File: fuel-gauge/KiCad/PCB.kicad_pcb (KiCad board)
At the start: 2 copper layers, 100.1 x 70 mm, 39 parts, among them P1 CONN_01X04, P2 CONN_01X04, P3 CONN_01X04, Q1 BSS84, Q2 BSS138, Q3 2N7002, SW1 Switch_SPDT_x2, U1 AQV252G, U2 SN74LVC1G08DBVR, U3 TLV3691IDCKR, U4 bq34z100pw

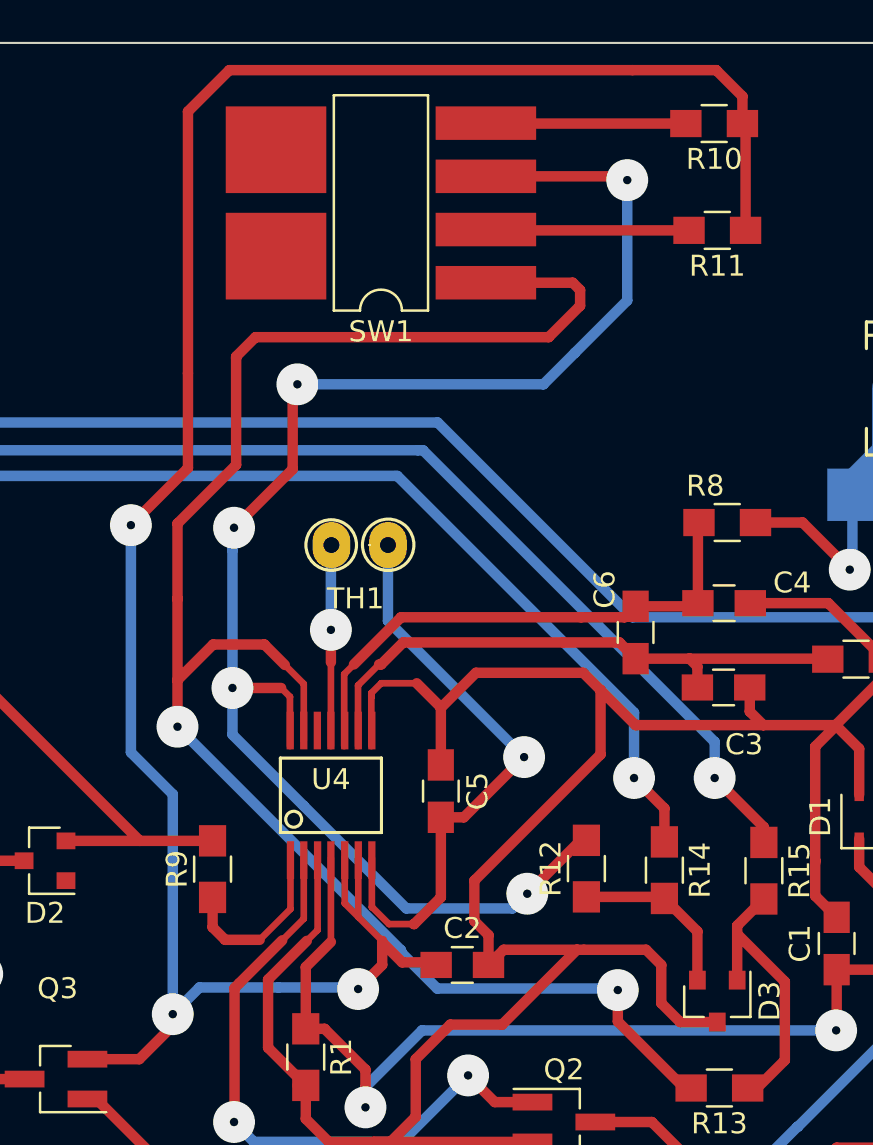
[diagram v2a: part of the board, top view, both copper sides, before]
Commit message: Correct the footprint of the switch 1
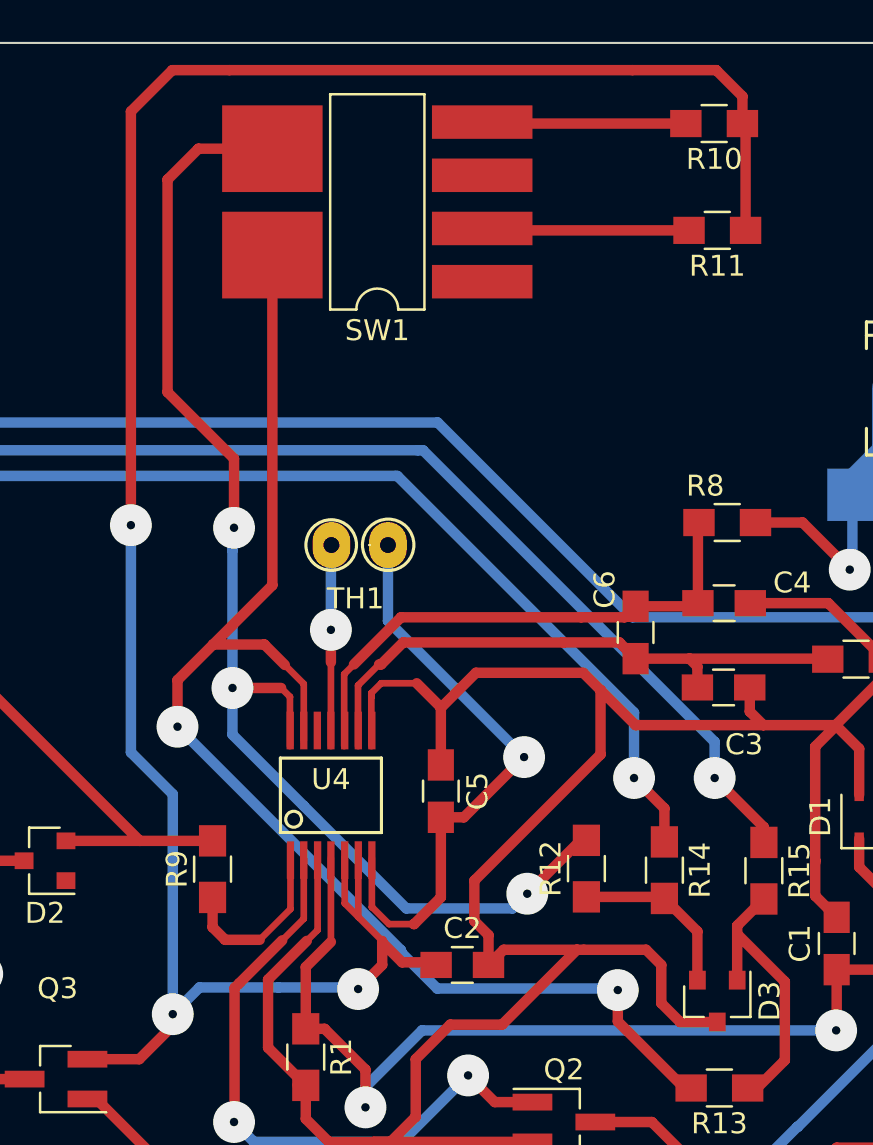
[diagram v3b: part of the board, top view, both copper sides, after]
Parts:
- moved SW1 0.18 mm to (157.6, 71.3)
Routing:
- net Net-(R13-Pad2): track 84.6 -> 64.9 mm
- net Net-(R12-Pad2): track 75.0 -> 60.5 mm, vias 5 -> 3
- net REG_IN: track 107.8 -> 109.4 mm

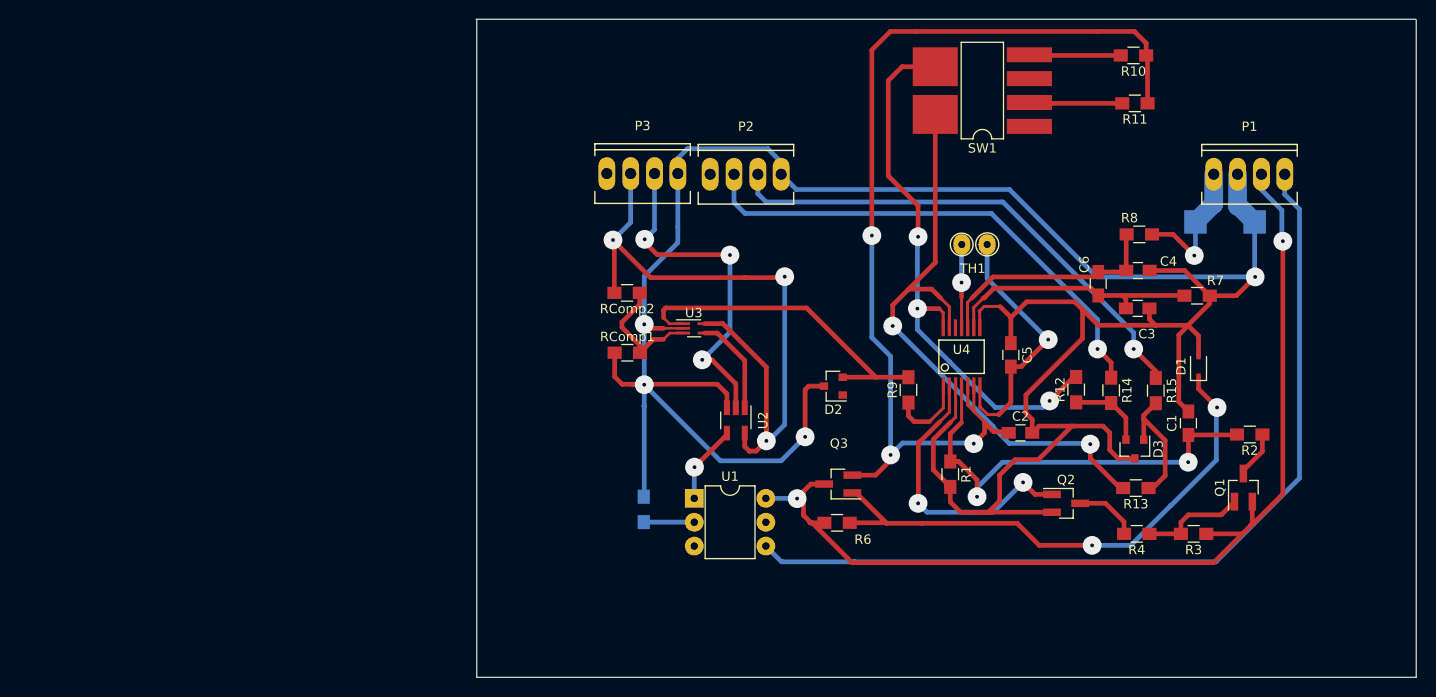
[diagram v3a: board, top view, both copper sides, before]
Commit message: Update the design to the v2
Include new routing to minimize the number of vias used and some
electrical considerations. Also the names of the connectors and the
positions of the switch.
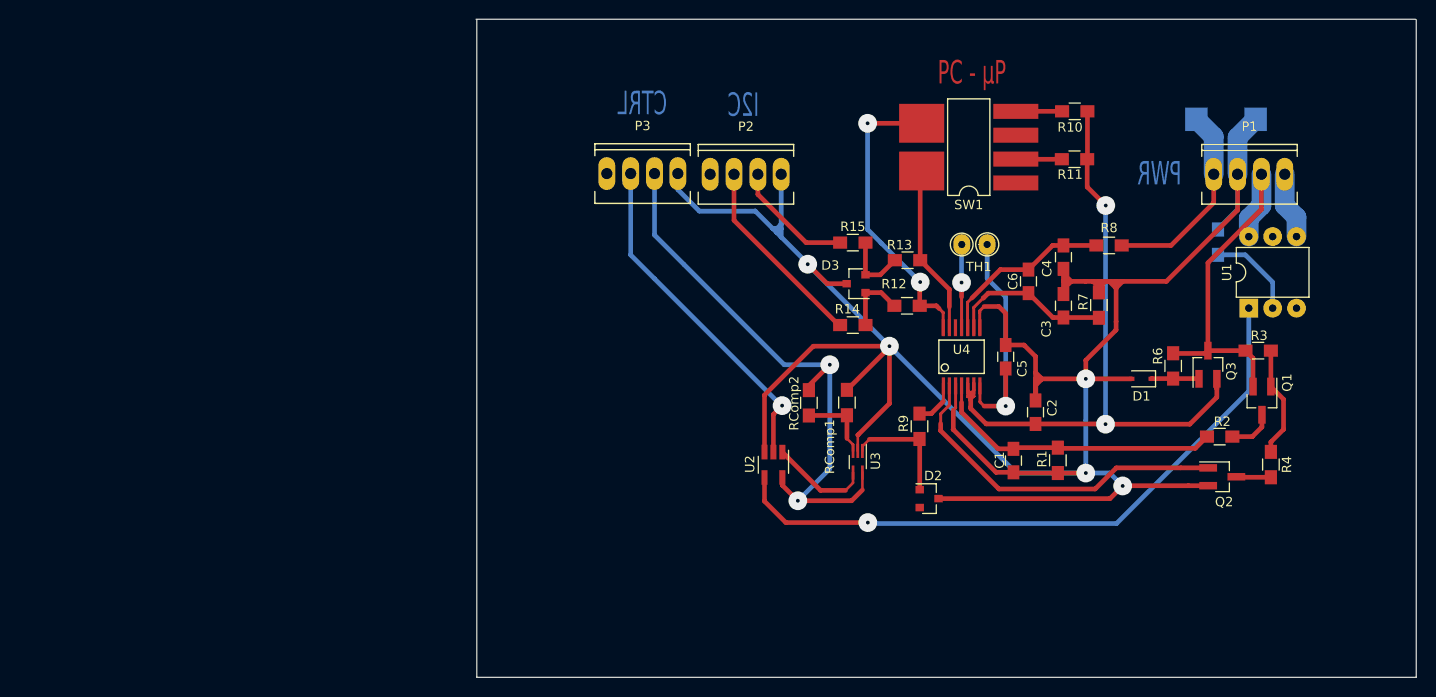
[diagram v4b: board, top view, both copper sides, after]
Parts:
- moved RRy1 67.4 mm to (178.9, 83.7)
- moved U1 62.4 mm to (182.2, 90.7), turned to 90 degrees
- moved Q3 41.3 mm to (177.8, 96.7), turned to 90 degrees
- moved R6 39.5 mm to (174.1, 96.8), turned to 270 degrees
- moved R15 35.9 mm to (140.0, 83.7), turned to 0 degrees
- moved D3 34.5 mm to (140.4, 88.1), turned to 180 degrees
- moved R13 34.3 mm to (145.8, 85.6), turned to 0 degrees
- moved R14 28.4 mm to (140.0, 92.5), turned to 0 degrees
- moved RComp1 24.0 mm to (139.4, 100.8), turned to 270 degrees
- moved RComp2 22.6 mm to (135.3, 100.8), turned to 90 degrees
- moved U3 22.1 mm to (140.3, 107.0), turned to 270 degrees
- moved R3 20.7 mm to (183.2, 95.2), turned to 0 degrees
- moved R12 20.1 mm to (145.8, 90.5), turned to 0 degrees
- moved C1 19.0 mm to (157.1, 106.9), turned to 270 degrees
- moved Q2 16.9 mm to (179.3, 108.7)
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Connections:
- D2 pad 1: Net-(D2-Pad1) -> (no net)
- D2 pad 2: (no net) -> Net-(D2-Pad2)
- P3 pad 2: +5V -> Net-(P3-Pad2)
- P3 pad 3: Net-(P3-Pad3) -> +5V
- R12 pad 1: Net-(D3-Pad1) -> Net-(D3-Pad2)
- R13 pad 1: Net-(D3-Pad2) -> Net-(D3-Pad1)
- R14 pad 2: Net-(D3-Pad1) -> Net-(D3-Pad2)
- R15 pad 2: Net-(D3-Pad2) -> Net-(D3-Pad1)
- R9 pad 2: Net-(D2-Pad1) -> Net-(D2-Pad2)
- U2 pad 2: Net-(P3-Pad3) -> Net-(P3-Pad2)
- U3 pad 1: Net-(D2-Pad1) -> Net-(D2-Pad2)
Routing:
- net /PUSHBUTTON: track 94.3 -> 8.14 mm
- net /BATT+: track 110.2 -> 40.3 mm, vias 2 -> 0
- net Net-(U1-Pad1): track 8.39 -> 69.7 mm
- net Net-(D1-Pad1): track 58.6 -> 5.10 mm, vias 2 -> 0
- net Net-(R13-Pad2): track 64.9 -> 18.5 mm, vias 2 -> 0
- net /SCL: track 54.0 -> 13.0 mm, vias 1 -> 0
- net Net-(P3-Pad3): track 36.9 -> 0.00 mm, vias 3 -> 0
- net Net-(P3-Pad2): track 0.00 -> 36.8 mm, vias 0 -> 1
- net Net-(D2-Pad1): track 35.9 -> 0.00 mm
- net REG_IN: track 109.4 -> 75.2 mm, vias 3 -> 2
- net /SDA: track 53.6 -> 20.8 mm, vias 1 -> 0
- net GNDREF: track 302.6 -> 272.9 mm, vias 4 -> 5
- net Net-(R12-Pad2): track 60.5 -> 32.7 mm, vias 3 -> 2
- net Net-(C1-Pad1): track 46.8 -> 31.4 mm, vias 2 -> 0
- net Net-(D2-Pad2): track 0.00 -> 12.3 mm
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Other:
- board text added: "CTRL"
- board text added: "I2C"
- board text added: "PC - µP"
- board text added: "PWR"
